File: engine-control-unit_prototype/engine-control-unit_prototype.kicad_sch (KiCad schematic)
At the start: 208 parts, among them IC1 TPS259573DSGR, J1 JTAG, J10 PORT_B, J11 PORT_C, J12 PORT_D, J13 PORT_A, J14 PORT_G, J15 PORT_F, J16 PORT_E, J17 2S_18650, J2 USB_C_Receptacle_USB2.0_man, J3 Micro_SD_Card_Det1, J4 PT1, J5 VREF, J6 PT1, J7 VREF, J8 FDCAN, U1 USBLC6-2SC6, U10 TPS55285, U13 INA219AxD, U14 LT3042xMSE, U3 INA826, U4 INA826, U5 TCAN337G, U6 INA219AxD, U7 STM32H747II, U8 INA219AxD, U9 TPS55285, Y1 32.768KHz, Y2 25MHz

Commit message: Fixed layout a bit
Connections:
- net GND: now also R4.2; no longer R4.1
- net at J2.B5 (CC2): now also R4.1; no longer R4.2
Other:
- note added: "CURRENT SENSE"
- note removed: "PSENSE"
- note removed: "PT PAS MIS, À VOIR"
- moved on the sheet: BZ1, C30, C31, C32, C40, C41, C46, C47, C48, C49, C50, C51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

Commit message: More layout cleanup
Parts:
- removed C31: 10uF/50V, Capacitor_SMD:CP_Elec_4x5.4, symbol Device:C_Polarized
- added C31: 10uF/50V, symbol Device:C_Polarized_US
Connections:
- net +5V: now also C31.1
- net GND: now also C31.2
- net Psense2_IN+: now also C83.1; no longer C81.1
- net VBAT_SAFE: now also C81.1; no longer C82.1
- net TPS10V_SCL: now reaches U9.2 (SCL)
- net TPS10V_SDA: now reaches U9.3 (SDA)
- net at U10.13 (VCC): now also C82.1; no longer C83.1
- net TPS3V3_SCL: now reaches U10.2 (SCL)
- net TPS3V3_SDA: now reaches U10.3 (SDA)
- net CLK_SD1 renamed SD_CLK
- net CMD_SD1 renamed SD_CMD
- net DAT0_SD1 renamed SD_DAT0
- net DAT1_SD1 renamed SD_DAT1
- net DAT2_SD1 renamed SD_DAT2
- net DAT3_SD1 renamed SD_DAT3
- net DET_SD1 renamed SD_DET
- removed net SCL: U13.4 (SCL), U6.4 (SCL), U8.4 (SCL)
- removed net SDA: U13.3 (SDA), U6.3 (SDA), U8.3 (SDA)
- new net CM1_SCL: U6.4 (SCL)
- new net CM1_SDA: U6.3 (SDA)
- new net CM2_SCL: U8.4 (SCL)
- new net CM2_SDA: U8.3 (SDA)
- new net CM3_SCL: U13.4 (SCL)
- new net CM3_SDA: U13.3 (SDA)
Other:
- note added: "CURRENT MONITOR"
- note added: "PINS TO MAP"
- note added: "TOUT LES LIENS GND/ALIM À FAIRE"
- note removed: "CURRENT SENSE"
- moved on the sheet: C32, C41, C47, C48, C49, C50, C51, C52, C54, C55, C56, C57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

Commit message: Added ADXL345 Accelerometer
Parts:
- added J9: ADXL345_CONN, symbol Connector:Conn_01x09_Socket
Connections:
- net +3V3: now also J9.2 (Pin_2)
- net GND: now also J9.1 (Pin_1)
- new net ADXL_CS: J9.3 (Pin_3)
- new net ADXL_SCL: J9.9 (Pin_9)
- new net ADXL_SDA: J9.8 (Pin_8)
- new net ADXL_SDO: J9.7 (Pin_7)
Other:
- note added: "ACCELEROMETER"
- note added: "PORTS"
- moved on the sheet: BZ1, C47, C48, C49, C50, C51, C52, J1, U2A

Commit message: Added valve control
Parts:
- added C86, C88: 1uF, Capacitor_SMD:C_0603_1608Metric_Pad1.08x0.95mm_HandSolder, symbol 0CSL_D1_V1:CAP_0.47uF_50V_0603
- added C87, C89: 0.1uF, Capacitor_SMD:C_0603_1608Metric_Pad1.08x0.95mm_HandSolder, symbol 0CSL_D1_V1:CAP_0.47uF_50V_0603
- added D4, D5: BAV99, Package_TO_SOT_SMD:SOT-23, symbol Diode:BAV99
- added F2, F3: Fuse, Fuse:Fuse_1206_3216Metric_Pad1.42x1.75mm_HandSolder, symbol Device:Fuse
- added J18: VALVE_IPA, symbol Connector:Screw_Terminal_01x03
- added J19: VALVE_NOS, symbol Connector:Screw_Terminal_01x03
- added J20: HEATER_IPA, symbol Connector:Screw_Terminal_01x02
- added J21: HEATER_NOS, symbol Connector:Screw_Terminal_01x02
- added J36: MTR_PWR, UserFootprints:CON_436500613, symbol Connector_Generic_MountingPin:Conn_01x06_MountingPin
- added R65, R66: 10k, Resistor_SMD:R_0603_1608Metric_Pad0.98x0.95mm_HandSolder, symbol 0CSL_D1_V1:RES0603
- added R67: R_US, symbol Device:R_US
- J9: value ADXL345_CONN -> ADXL345
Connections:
- net +3V3: now also D4.2 (A), D5.2 (A)
- net GND: now also C86.2, C87.2, C88.2, C89.2, D4.1 (K), D5.1 (K), J18.3 (Pin_3), J19.3 (Pin_3), J36.4 (Pin_4), J36.5 (Pin_5), J36.6 (Pin_6), J36.MP (MountPin), R65.2, R66.2
- net TCAN_FLT: now reaches U5.5 (FAULT)
- net at BZ1.1: now also R67.2
- new net: C86.1, C87.1, F2.2, J18.2 (Pin_2)
- new net: C88.1, C89.1, F3.2, J19.2 (Pin_2)
- new net BUZZ: R67.1
- new net DATA_S1: D4.3 (K), D5.3 (K), J18.1 (Pin_1), J19.1 (Pin_1), R65.1, R66.1
- new net Vdrive: F2.1, F3.1, J36.1 (Pin_1), J36.2 (Pin_2), J36.3 (Pin_3)
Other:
- note added: "ADD OTHER ADC TO TEST (MATIS)"
- note added: "Check EN and FB pins function"
- note added: "PULL_PIN ?"
- note added: "VALVE CONTROL"
- moved on the sheet: C40, C41, C46, C53, C54, C55, C56, C57, J8, J9, R13, R22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

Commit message: Changed location of PINS TO MAP to PORTS Changed location of JTAG to USB-C/PROG Added Thermistors (ca parait du que le cours d'innov est intéressant ?)
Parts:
- added C90, C91: 1uF, Capacitor_SMD:C_0603_1608Metric_Pad1.08x0.95mm_HandSolder, symbol Device:C
- added J22: THERM2, UserFootprints:MOLEX_5013310207, symbol Connector_Generic_MountingPin:Conn_01x02_MountingPin
- added J26: THERM1, UserFootprints:MOLEX_5013310207, symbol Connector_Generic_MountingPin:Conn_01x02_MountingPin
- added R68, R69: 10k, Resistor_SMD:R_0603_1608Metric_Pad0.98x0.95mm_HandSolder, symbol Device:R
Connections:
- net +3V3: now also J22.1 (Pin_1), J26.1 (Pin_1)
- net DATA_S1: no longer D5.3 (K), J19.1 (Pin_1), R66.1
- net GND: now also C90.2, C91.2, J22.MP (MountPin), J26.MP (MountPin), R68.2, R69.2
- new net DATA_S2: D5.3 (K), J19.1 (Pin_1), R66.1
- new net THERM1: C90.1, J26.2 (Pin_2), R68.1
- new net THERM2: C91.1, J22.2 (Pin_2), R69.1
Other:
- note added: "Dont forget to add heater control and magnetic encoder"
- note added: "THERMISTORS"
- note added: "USB-C/PROG"
- note removed: "USB-C"
- moved on the sheet: BZ1, J1, R67

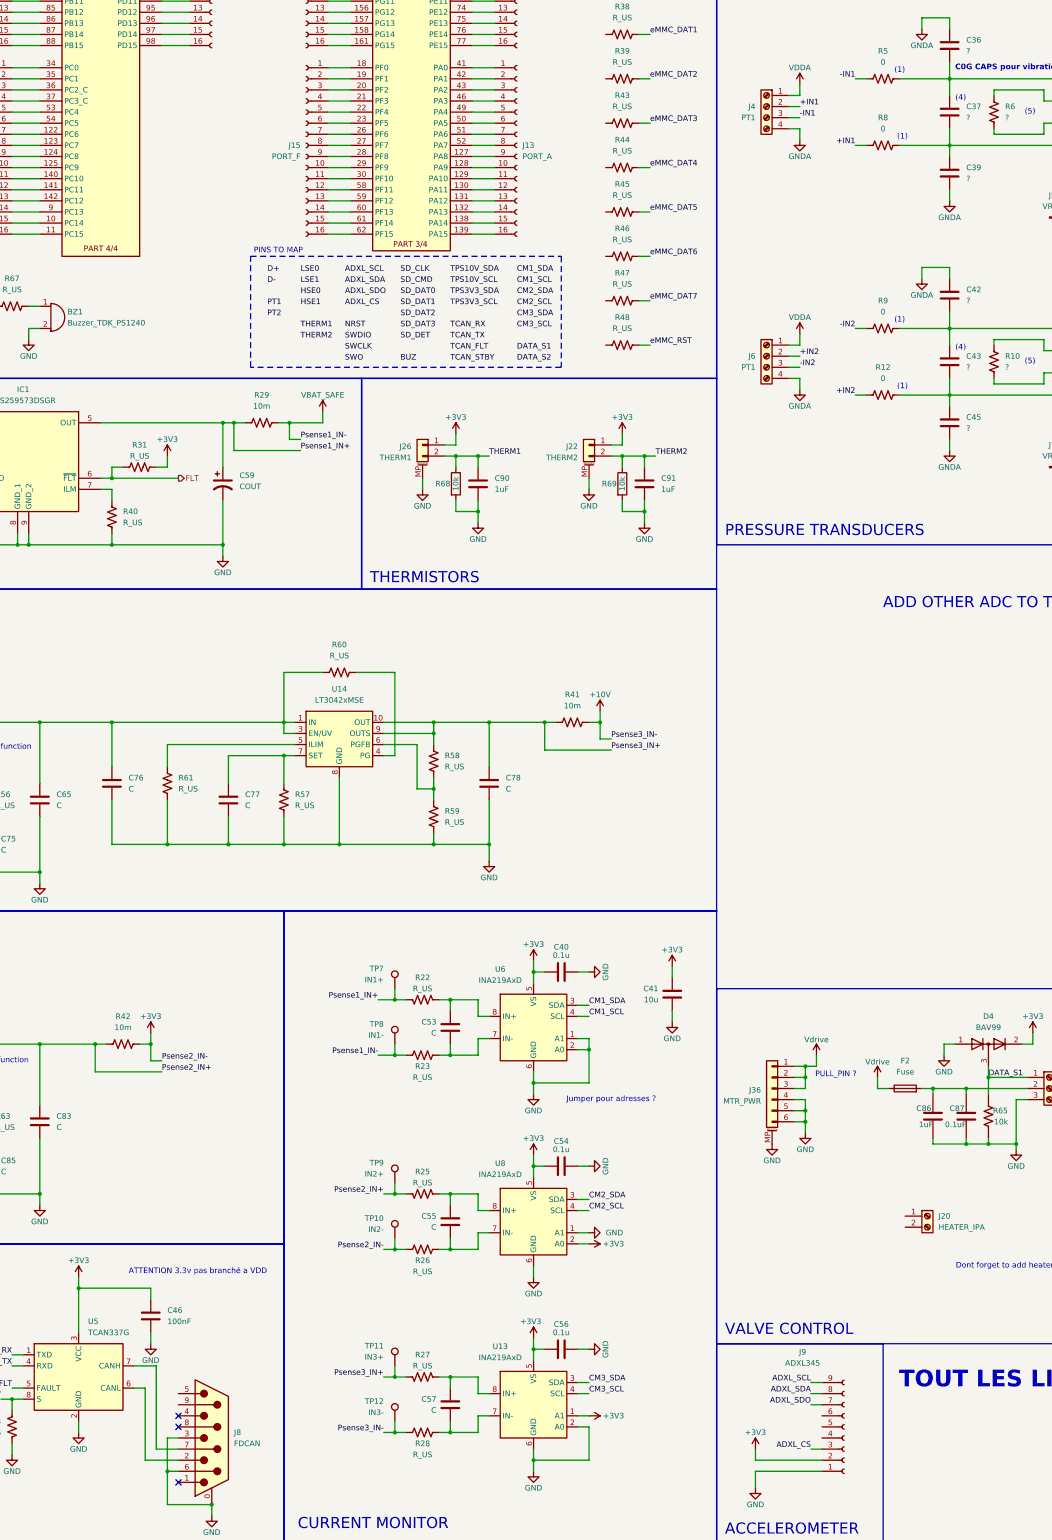
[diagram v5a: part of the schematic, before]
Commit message: Added magnetic connector
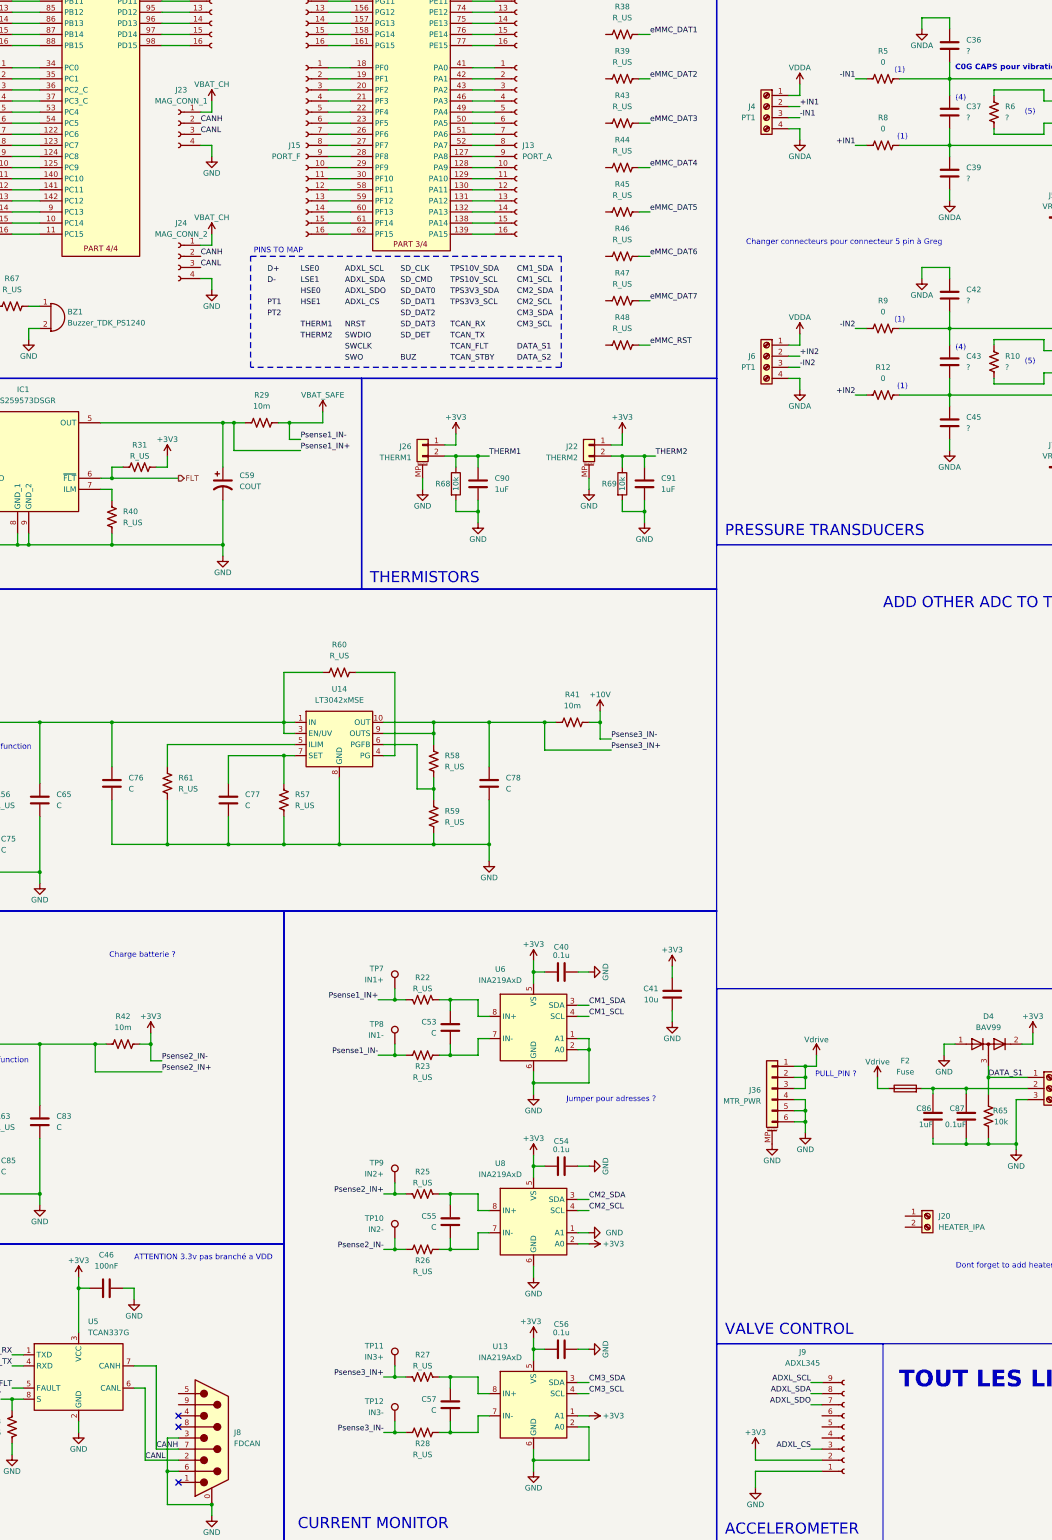
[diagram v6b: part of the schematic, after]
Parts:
- added J23: MAG_CONN_1, symbol Connector:Conn_01x04_Socket
- added J24: MAG_CONN_2, symbol Connector:Conn_01x04_Socket
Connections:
- net GND: now also J23.4 (Pin_4), J24.4 (Pin_4)
- net CANL: now reaches J8.2, U5.6 (CANL)
- net CANL: now also J23.3 (Pin_3), J24.3 (Pin_3)
- net CANH: now reaches J8.7, U5.7 (CANH)
- net CANH: now also J23.2 (Pin_2), J24.2 (Pin_2)
- new net VBAT_CH: J23.1 (Pin_1), J24.1 (Pin_1)
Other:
- note added: "Changer connecteurs pour connecteur 5 pin à Greg"
- note added: "Charge batterie ?"
- moved on the sheet: C46

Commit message: Fixed some of the issues from design review Added heater circuit Added buzzer circuit (I know layout wierd rn, it will be fixed later)
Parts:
- removed C86, C88: 1uF, Capacitor_SMD:C_0603_1608Metric_Pad1.08x0.95mm_HandSolder, symbol 0CSL_D1_V1:CAP_0.47uF_50V_0603
- removed C87, C89: 0.1uF, Capacitor_SMD:C_0603_1608Metric_Pad1.08x0.95mm_HandSolder, symbol 0CSL_D1_V1:CAP_0.47uF_50V_0603
- removed F2, F3: Fuse, Fuse:Fuse_1206_3216Metric_Pad1.42x1.75mm_HandSolder, symbol Device:Fuse
- removed J36: MTR_PWR, UserFootprints:CON_436500613, symbol Connector_Generic_MountingPin:Conn_01x06_MountingPin
- removed R1, R2: 0, symbol Device:R
- added C86, C87, C88, C92: 0.1u, symbol Device:C
- added D6: D_Zener, symbol Device:D_Zener
- added J25: I2C_A, symbol Connector:Conn_01x04_Socket
- added J27: I2C_B, symbol Connector:Conn_01x04_Socket
- added J28: I2C_C, symbol Connector:Conn_01x04_Socket
- added J29: I2C_D, symbol Connector:Conn_01x04_Socket
- added Q1: PMOS, symbol Simulation_SPICE:PMOS
- added Q2, Q4: NMOS, symbol Simulation_SPICE:NMOS
- added Q3, Q5, Q6: NPN, symbol Simulation_SPICE:NPN
- added R1, R100, R101, R102, R103, R104, R105, R106, R107, R108, R109, R110, R111, R112, R113, R114, R115, R116, R117, R118, R119, R120, R121, R122, R123, R124, R125, R126, R127, R128, R129, R130, R131, R132, R133, R134, R135, R136, R137, R138, R139, R140, R141, R142, R143, R2, R77, R78, R79, R80, R95, R96, R97, R98, R99: 0, symbol Device:R_US
- added R70, R71, R72, R73, R74, R75, R76, R83, R84, R85, R86, R87, R88, R89, R90, R91, R92, R93, R94: R_US, symbol Device:R_US
- added R81, R82: 60, symbol Device:R_US
- added SW1: BOOT, symbol Switch:SW_Push_SPDT
- C38: value C -> DNF
- D1: footprint Diode_SMD:D_0603_1608Metric_Pad1.05x0.95mm_HandSolder -> (none); Part Number 5399-BAT760CT-ND -> (none)
- R34, R35, R36, R38, R39, R43, R44, R45, R46, R47, R48: value R_US -> 22
- R60: value R_US -> 200k
- R62: value 10k -> DNF
- R67: value R_US -> ?
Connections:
- net VDD55_USB is gone; now on net VDD50_USB: C29.1, U7.120 (VDD50_USB)
- net VSSA is gone; now on net GND: U7.38 (VSSA)
- net VSSDSI is gone; now on net GND: C26.2, C27.2, U7.105 (VSSDSI), U7.109 (VSSDSI)
- net VSSSMPS is gone; now on net GND: C67.2, C70.2, C71.2, C72.2, C73.2, C74.2, U7.14 (VSSSMPS)
- net +3V3: no longer C40.2, C46.1, C54.2, C56.2, D4.2 (A), D5.2 (A), J1.1 (Pin_1), J22.1 (Pin_1), J26.1 (Pin_1), J9.2 (Pin_2), R26.2, R42.2, R49.1, R50.1, R51.1, R52.1, R53.1, R54.1, R62.1, TP10.1, U13.5 (VS), U5.3 (VCC), U6.5 (VS), U8.5 (VS)
- net +5V: no longer C30.1, C31.1, D1.1 (K)
- net +BATT1: now also J20.1 (Pin_1), J21.1 (Pin_1), R71.1, R73.1
- net ADXL_CS: now also R114.2
- net ADXL_SCL: now also R111.2
- net ADXL_SDA: now also R112.2
- net ADXL_SDO: now also R113.2
- net BOOT0: now also SW1.2 (B)
- net BUZ: now also R124.2
- net BUZZ: now also R75.1; no longer R67.1
- net CANH: now also R81.1
- net CANL: now also R82.1
- net D+: now also R136.2
- net D-: now also R137.2
- net DATA_S1: now also R122.2
- net DATA_S2: now also J19.2 (Pin_2), R123.2; no longer J19.1 (Pin_1)
- net GND: now also R67.1, U7.174 (PDR_ON), C86.1, C87.1, C88.1, C92.2, J25.1 (Pin_1), J27.1 (Pin_1), J28.1 (Pin_1), J29.1 (Pin_1), Q2.3 (S), Q3.3 (E), Q4.3 (S), Q5.3 (E), Q6.3 (E), R140.2, R70.2, R78.1, R89.2, R92.2, SW1.1 (A); no longer BZ1.2, J3.10 (SHIELD), J8.0 (PAD), J9.1 (Pin_1)
- net GNDA: now also R140.1
- net HSE0: now also R131.2
- net HSE1: now also R132.2
- net LSE0: now also R129.2
- net LSE1: now also R130.2
- net NRST: now also R125.2
- net PT1: now also R133.2
- net PT2: now also R134.2
- net SD_CLK: now also R79.2
- net SD_CMD: now also R80.2
- net SD_DAT0: now also R95.2
- net SD_DAT1: now also R96.2
- net SD_DAT2: now also R115.2
- net SD_DAT3: now also R116.2
- net SD_DET: now also R117.2
- net SWCLK: now also R127.2
- net SWDIO: now also R126.2
- net SWO: now also R128.2
- net TCAN_FLT: now also R120.2
- net TCAN_RX: now also R118.2
- net TCAN_STBY: now also R121.2
- net TCAN_TX: now also R119.2
- net THERM1: now also R109.2
- net THERM2: now also R110.2
- net TPS10V_SCL: now also J27.4 (Pin_4), R106.2, R86.2
- net TPS10V_SDA: now also J27.3 (Pin_3), R105.2, R85.2
- net TPS3V3_SCL: now also J25.4 (Pin_4), R104.2, R88.2
- net TPS3V3_SDA: now also J25.3 (Pin_3), R103.2, R87.2
- net VBAT_SAFE: now also R90.1, R91.1
- net VDD33_USB: now also D1.2 (A), R138.1
- net VDD50_USB: now also R138.2
- net VDDA: now also R1.2
- net VDDLDO: now also U7.135 (VDDLDO), U7.82 (VDDLDO)
- net VDD_MCU: now also R1.1, R139.1, R2.1, SW1.3 (C); no longer JP5.1 (A), L3.1
- net VREF+: now also R2.2
- net eMMC_CLK: no longer R24.2, R35.2, U2.M5 (CMD)
- net TPS3V3_INT: now reaches U10.10 (FB/INT)
- net TPS3V3_INT: now also R143.2
- net at U10.4 (EN/UVLO): now also R89.1, R90.2
- net at J21.2 (Pin_2): now also Q4.1 (D)
- net at R67.2: no longer names the net of R67.2
- net at R67.2: now also U2.H5 (DS); no longer BZ1.1
- net at U7.31 (PH0): now also R131.1
- net at U7.32 (PH1): now also R132.1
- net TPS10V_INT: now reaches U9.10 (FB/INT)
- net TPS10V_INT: now also R142.2
- net at U9.4 (EN/UVLO): now also R91.2, R92.1
- net at J2.S1 (SHIELD): now also C86.2
- net at D2.1 (K), F1.2: now also Q1.1 (D); no longer D1.2 (A)
- net at J20.2 (Pin_2): now also Q2.1 (D)
- net +10V renamed VDD_10V
- net CM1_SCL: no longer names the net of U6.4 (SCL)
- net CM1_SCL: now also R98.1
- net CM1_SDA: no longer names the net of U6.3 (SDA)
- net CM1_SDA: now also R97.1
- net CM2_SCL: no longer names the net of U8.4 (SCL)
- net CM2_SCL: now also R100.1
- net CM2_SDA: no longer names the net of U8.3 (SDA)
- net CM2_SDA: now also R99.1
- net CM3_SCL: no longer names the net of U13.4 (SCL)
- net CM3_SCL: now also R102.1
- net CM3_SDA: no longer names the net of U13.3 (SDA)
- net CM3_SDA: now also R101.1
- net FLT renamed EFUSE_FLT
- net EFUSE_FLT: now also R141.2
- net VBAT_CH: no longer names the net of J24.1 (Pin_1)
- net VBAT_CH: no longer J23.1 (Pin_1)
- net VDD renamed VDD_3V3
- net VDD_3V3: now also C40.2, C46.1, C54.2, C56.2, D1.1 (K), D4.2 (A), D5.2 (A), J1.1 (Pin_1), J22.1 (Pin_1), J26.1 (Pin_1), JP5.1 (A), L3.1, R26.2, R42.2, R49.1, R50.1, R51.1, R52.1, R53.1, R54.1, R62.1, TP10.1, U13.5 (VS), U5.3 (VCC), U6.5 (VS), U8.5 (VS), J25.2 (Pin_2), J27.2 (Pin_2), J28.2 (Pin_2), J29.2 (Pin_2), R139.2, R76.1, R77.1, R83.1, R84.1, R85.1, R86.1, R87.1, R88.1, R93.1, R94.1
- new net: C88.2, R81.2, R82.2
- new net: Q2.2 (G), Q3.1 (C), R71.2
- new net: C87.2, J8.0 (PAD)
- new net: BZ1.2, Q6.1 (C)
- new net: Q6.2 (B), R75.2
- new net: BZ1.1, R76.2
- new net: Q5.2 (B), R74.2
- new net: D6.2 (A), Q1.2 (G), R70.1
- new net: Q4.2 (G), Q5.1 (C), R73.2
- new net: Q3.2 (B), R72.2
- new net: J9.1 (Pin_1), R78.2
- new net: C92.1, J3.10 (SHIELD)
- new net: J9.2 (Pin_2), R77.2
- new net CM_SCL: J28.4 (Pin_4), R100.2, R102.2, R84.2, R98.2
- new net CM_SDA: J28.3 (Pin_3), R101.2, R83.2, R97.2, R99.2
- new net H_IPA: R72.1
- new net H_NOS: R74.1
- new net I2CD_SCL: J29.4 (Pin_4), R108.2, R94.2
- new net I2CD_SDA: J29.3 (Pin_3), R107.2, R93.2
- new net OTG_USB: R135.1
- new net VBUS: C30.1, C31.1, D6.1 (K), Q1.3 (S), R135.2
- new net eMMC_CMD: R24.2, R35.2, U2.M5 (CMD)
- no-connect marks 13 -> 21
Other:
- note added: "Dont forget to add magnetic encoder"
- note added: "Loop du vdd ou non ?"
- note added: "POWER/CURRENT MONITOR"
- note added: "Power ? Ou 10V enough ?"
- note added: "Ringing resistor (near mcu)"
- note removed: "ACCELEROMETER"
- note removed: "ATTENTION 3.3v pas branché a VDD"
- note removed: "CURRENT MONITOR"
- note removed: "Charge batterie ?"
- note removed: "Check EN and FB pins function"
- note removed: "Dont forget to add heater control and magnetic encoder"
- note removed: "PULL_PIN ?"
- note removed: "Ringing resistor"
- note removed: "TOUT LES LIENS GND/ALIM À FAIRE"
- note removed: "VALVE CONTROL"
- moved on the sheet: BZ1, C22, C23, C28, C29, C30, C31, C32, C34, C40, C41, C46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

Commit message: Added test points
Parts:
- added TP1: PT1, symbol Connector:TestPoint
- added TP13: VDD_3V3, symbol Connector:TestPoint
- added TP14: CANH, symbol Connector:TestPoint
- added TP15: CANL, symbol Connector:TestPoint
- added TP16: TH1, symbol Connector:TestPoint
- added TP17: TH2, symbol Connector:TestPoint
- added TP18: S1, symbol Connector:TestPoint
- added TP19: S2, symbol Connector:TestPoint
- added TP2: PT2, symbol Connector:TestPoint
- added TP3: VDD_10V, symbol Connector:TestPoint
- added TP4: TPS10V_OUT, symbol Connector:TestPoint
- added TP5: BATT1, symbol Connector:TestPoint
- added TP6: VBATT_SAFE, symbol Connector:TestPoint
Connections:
- net +BATT1: now also TP5.1
- net CANH: now also TP14.1
- net CANL: now also TP15.1
- net DATA_S1: now also TP18.1
- net DATA_S2: now also TP19.1
- net THERM1: now also TP16.1
- net THERM2: now also TP17.1
- net VBAT_SAFE: now also TP6.1
- net VDD_10V: now also TP3.1
- net VDD_3V3: now also TP13.1
- net at R11.2, U4.7 (Vout): now also TP2.1
- net at C65.1, C76.1, R60.1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: now also TP4.1
- net at R7.2, U3.7 (Vout): now also TP1.1
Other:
- note added: "C0G ?"
- note removed: "ADD OTHER ADC TO TEST (MATIS)"
- note removed: "C0G CAPS pour vibrations"
- moved on the sheet: C38, C44, C46, C90, C91, J22, J26, R11, R13, R136, R137, R142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
